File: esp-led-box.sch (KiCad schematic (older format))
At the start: 26 parts, among them J1 Conn_01x03, J2 Conn_01x02_Female, J3 Conn_01x03_Female, Q1 BSS138, U1 ESP-12F, U2 MP2307, U3 LM3940

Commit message: Fixed iteration #2
- replace 0603 SMDs with 1206 ones;
- add fuse holder
- add two ACT LEDs
- fix level shifter transistor scheme
- add degson terminal block
- use 2.56 pin header
- add GPIO0, +3.3v pins to pin header
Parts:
- added D1, D2: LED, LED_SMD:LED_1206_3216Metric, symbol Device:LED
- added D3: D, Diode_SMD:D_SOD-123, symbol Device:D
- added F1: Fuse, Fuse:Fuseholder_Blade_Mini_Keystone_3568, symbol Device:Fuse
- added R11, R12: 120, Resistor_SMD:R_1206_3216Metric, symbol Device:R
- C2, C4, C5, C6: footprint Capacitor_SMD:C_0603_1608Metric -> Capacitor_SMD:C_1206_3216Metric
- J1: footprint Connector_PinHeader_1.27mm:PinHeader_1x04_P1.27mm_Vertical -> Connector_PinHeader_2.54mm:PinHeader_1x06_P2.54mm_Vertical; symbol Connector_Generic:Conn_01x04 -> Connector_Generic:Conn_01x06
- J2: footprint Connector_PinHeader_1.27mm:PinHeader_1x02_P1.27mm_Vertical -> esp-light-box:WG235-2P
- J3: footprint Connector_PinHeader_1.27mm:PinHeader_1x03_P1.27mm_Vertical -> Connector_PinHeader_2.54mm:PinHeader_1x03_P2.54mm_Vertical
- R1, R10, R2, R3, R4, R5, R6, R7, R8, R9: footprint Resistor_SMD:R_0603_1608Metric -> Resistor_SMD:R_1206_3216Metric
- U1: symbol ESP8266:ESP-12F -> esp-led-box-rescue:ESP-12F-ESP8266
- U2: symbol mp2307:MP2307 -> esp-led-box-rescue:MP2307-mp2307
- U3: symbol lm3940:LM3940 -> esp-led-box-rescue:LM3940-lm3940
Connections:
- net labels added: GPIO0, GREEN_LED, RED_LED
- wire segments 60 -> 74
- no-connect marks 14 -> 12
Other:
- moved on the sheet: J2, Q1, R10, R3, R9

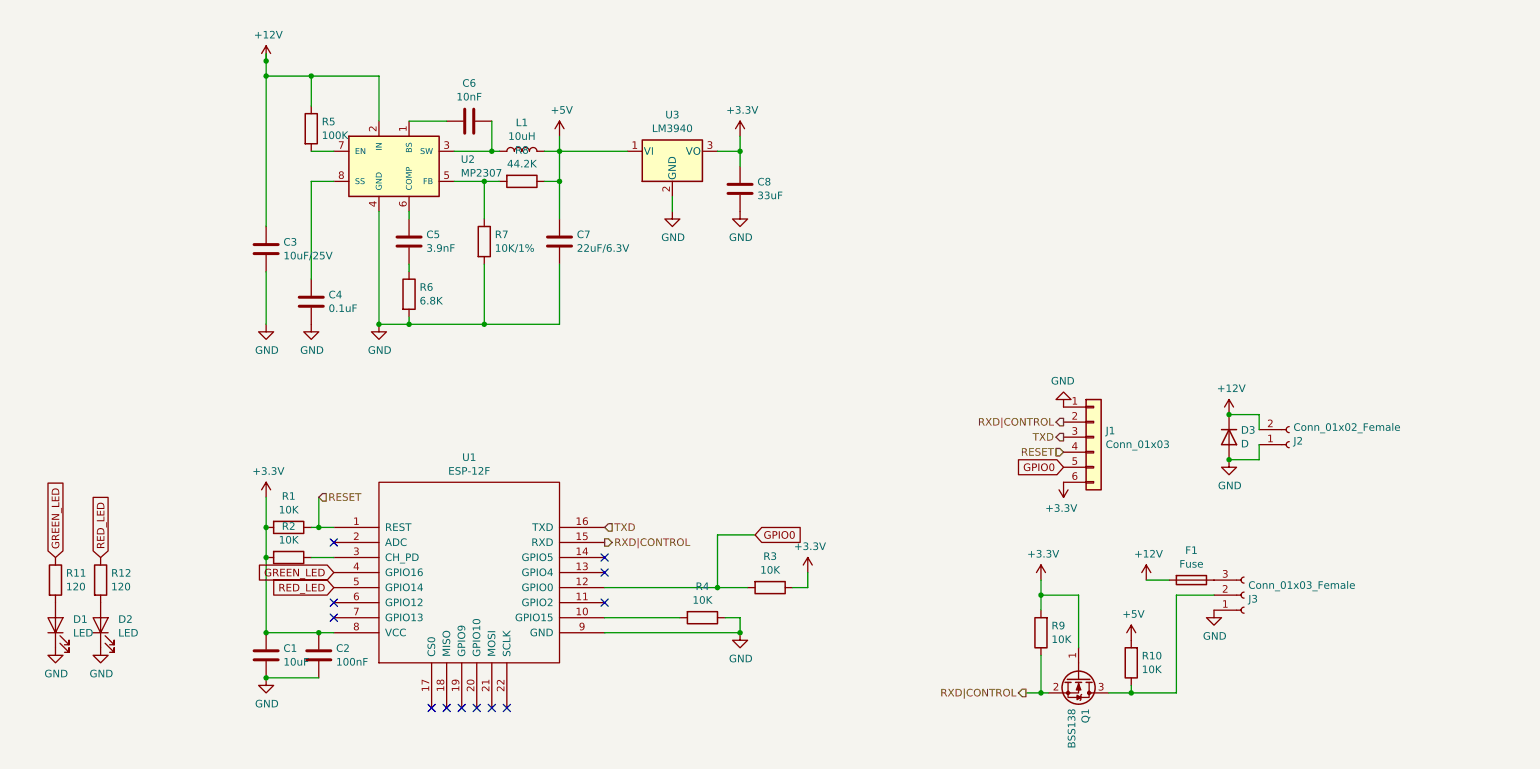
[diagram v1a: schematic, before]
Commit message: pcb: make ready for manufacturing
- dummy resistors to switch from +12v power input to +5v input to make box be usable with different LED strips
- some cosmetic changes withing .sch
- put protection diode inline not parallel
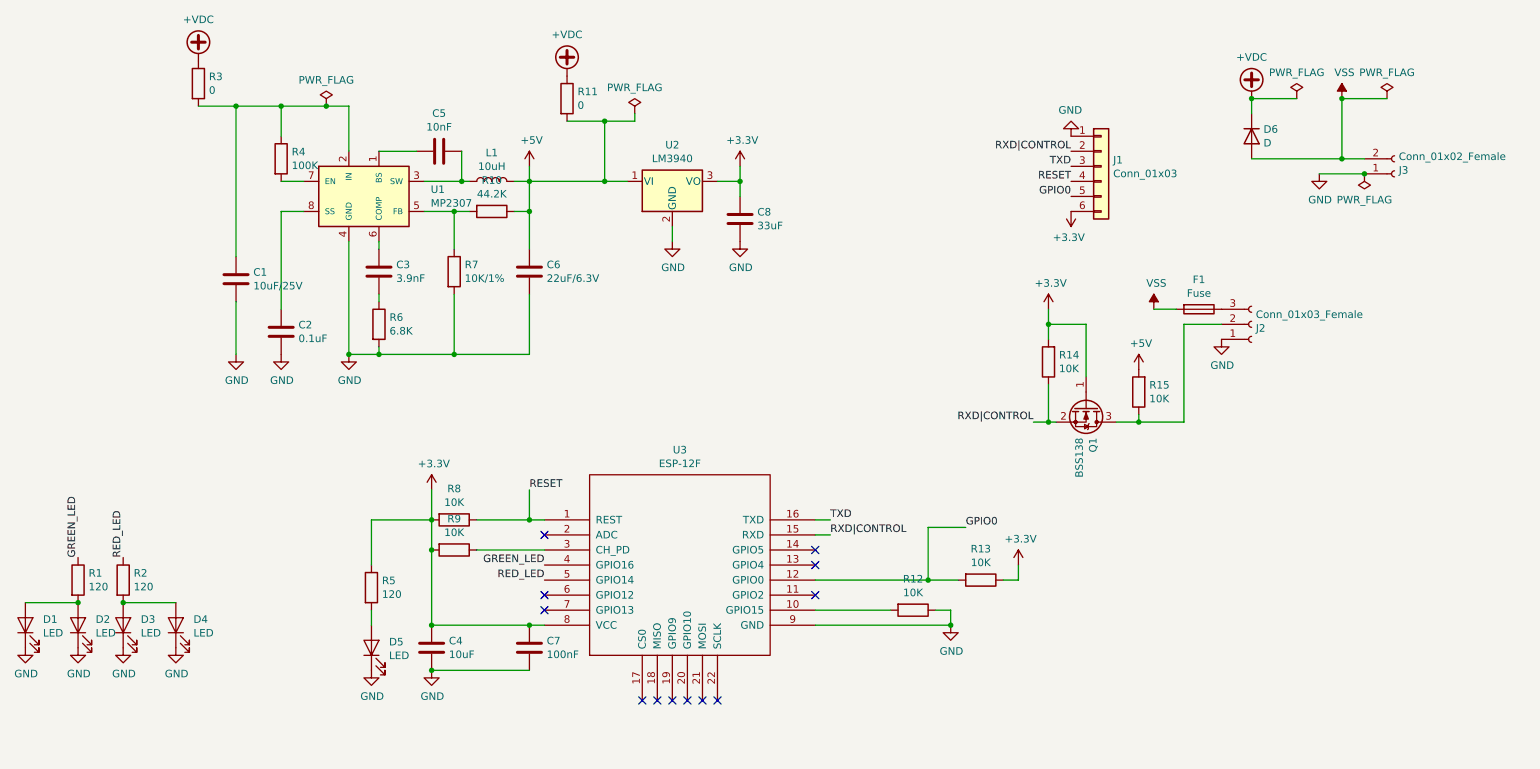
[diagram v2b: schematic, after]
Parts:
- added D1, D4, D5: LED, LED_SMD:LED_1206_3216Metric, symbol Device:LED
- added R11, R3: 0, Resistor_SMD:R_1206_3216Metric, symbol Device:R
- added R5: 120, Resistor_SMD:R_1206_3216Metric, symbol Device:R
- renumbered C3 to C1, C4 to C2, C5 to C3, C1 to C4, C6 to C5, C7 to C6, C2 to C7, D1 to D2, D2 to D3, D3 to D6, J3 to J2, J2 to J3, R11 to R1, R8 to R10, R4 to R12, R3 to R13, R9 to R14, R10 to R15, R12 to R2, R5 to R4, R1 to R8, R2 to R9, U2 to U1, U3 to U2, U1 to U3
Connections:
- net +3V3: now also R5.1
- net +5V: now also R11.2
- net GND: now also D1.1 (K), D4.1 (K), D5.1 (K); no longer D6.2 (A)
- net at D2.2 (A), R1.2: now also D1.2 (A)
- net at D3.2 (A), R2.2: now also D4.2 (A)
- net +12V: no longer names the net of C1.1, R4.1, U1.2 (IN)
- net +12V: now also R3.2; no longer D6.1 (K), F1.2, J3.2 (Pin_2)
- new net: D5.2 (A), R5.2
- new net +VDC: D6.1 (K), R11.1, R3.1
- new net VSS: D6.2 (A), F1.2, J3.2 (Pin_2)
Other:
- moved on the sheet: C1, C2, C3, C4, C5, C6, C7, C8, D2, D3, D6, F1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

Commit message: rework fuse holder: use one from aliexpress
https://aliexpress.ru/item/32838425418.html?spm=a2g0s.9042311.0.0.5f9933edQqCEM1 here is the link (it supposed to be used with micro blades fuses)
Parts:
- F1: footprint Fuse:Fuseholder_Blade_Mini_Keystone_3568 -> esp-light-box:fuseholder_blade_common_aliexpress
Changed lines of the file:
@@
 	1    0    0    -1
-$EndComp
-$Comp
-L Device:Fuse F1
-U 1 1 5E6D1E06
-P 8500 2800
-F 0 "F1" V 8303 2800 50  0000 C CNN
-F 1 "Fuse" V 8394 2800 50  0000 C CNN
-F 2 "Fuse:Fuseholder_Blade_Mini_Keystone_3568" V 8430 2800 50  0001 C CNN
-F 3 "~" H 8500 2800 50  0001 C CNN
-	1    8500 2800
-	0    1    1    0
 $EndComp
 Wire Wire Line
@@
 	4050 1950 4550 1950
 $Comp
-L power:VSS #PWR?
+L power:VSS #PWR0101
 U 1 1 5E906664
 P 9450 1400
-F 0 "#PWR?" H 9450 1250 50  0001 C CNN
+F 0 "#PWR0101" H 9450 1250 50  0001 C CNN
 F 1 "VSS" H 9467 1573 50  0000 C CNN
 F 2 "" H 9450 1400 50  0001 C CNN
@@
 $EndComp
 $Comp
-L power:PWR_FLAG #FLG?
+L power:PWR_FLAG #FLG0101
 U 1 1 5E907205
 P 9750 1400
-F 0 "#FLG?" H 9750 1475 50  0001 C CNN
+F 0 "#FLG0101" H 9750 1475 50  0001 C CNN
 F 1 "PWR_FLAG" H 9750 1573 50  0000 C CNN
 F 2 "" H 9750 1400 50  0001 C CNN
@@
 $EndComp
 $Comp
-L power:VSS #PWR?
+L power:VSS #PWR0102
 U 1 1 5E919360
 P 8200 2800
-F 0 "#PWR?" H 8200 2650 50  0001 C CNN
+F 0 "#PWR0102" H 8200 2650 50  0001 C CNN
 F 1 "VSS" H 8217 2973 50  0000 C CNN
 F 2 "" H 8200 2800 50  0001 C CNN
@@
 	1    0    0    -1
 $EndComp
+$Comp
+L Device:Fuse F1
+U 1 1 5E6D1E06
+P 8500 2800
+F 0 "F1" V 8303 2800 50  0000 C CNN
+F 1 "Fuse" V 8394 2800 50  0000 C CNN
+F 2 "esp-light-box:fuseholder_blade_common_aliexpress" V 8430 2800 50  0001 C CNN
+F 3 "~" H 8500 2800 50  0001 C CNN
+	1    8500 2800
+	0    1    1    0
+$EndComp
 $EndSCHEMATC

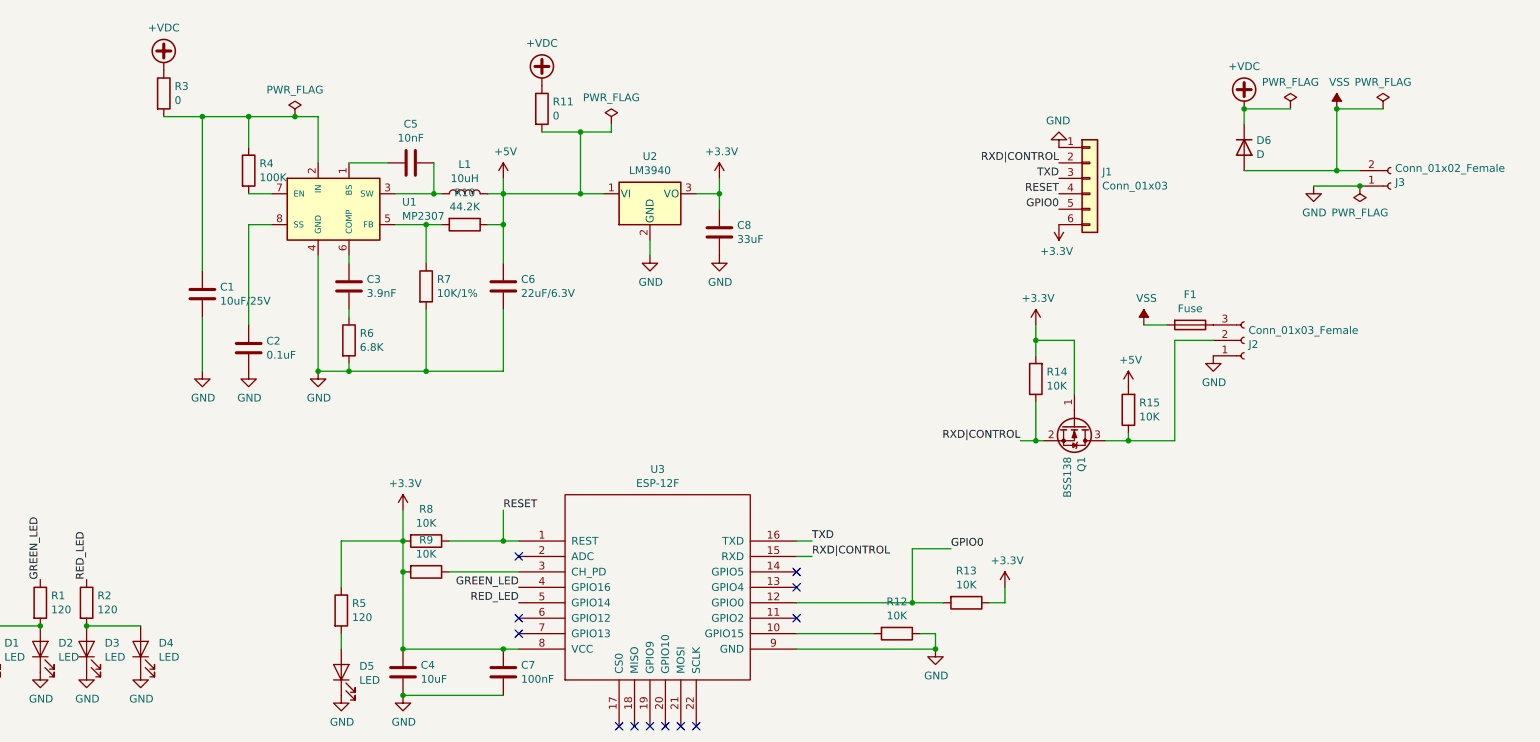
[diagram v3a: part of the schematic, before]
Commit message: pcb v0.3 update
- add possibility to use switch instead of dummy resisters
- add micro USB footprint for portable use
- add buttons for RESET and GPIO0 ESP inputs
- make it fancier with components density increased
- add case mountpoints
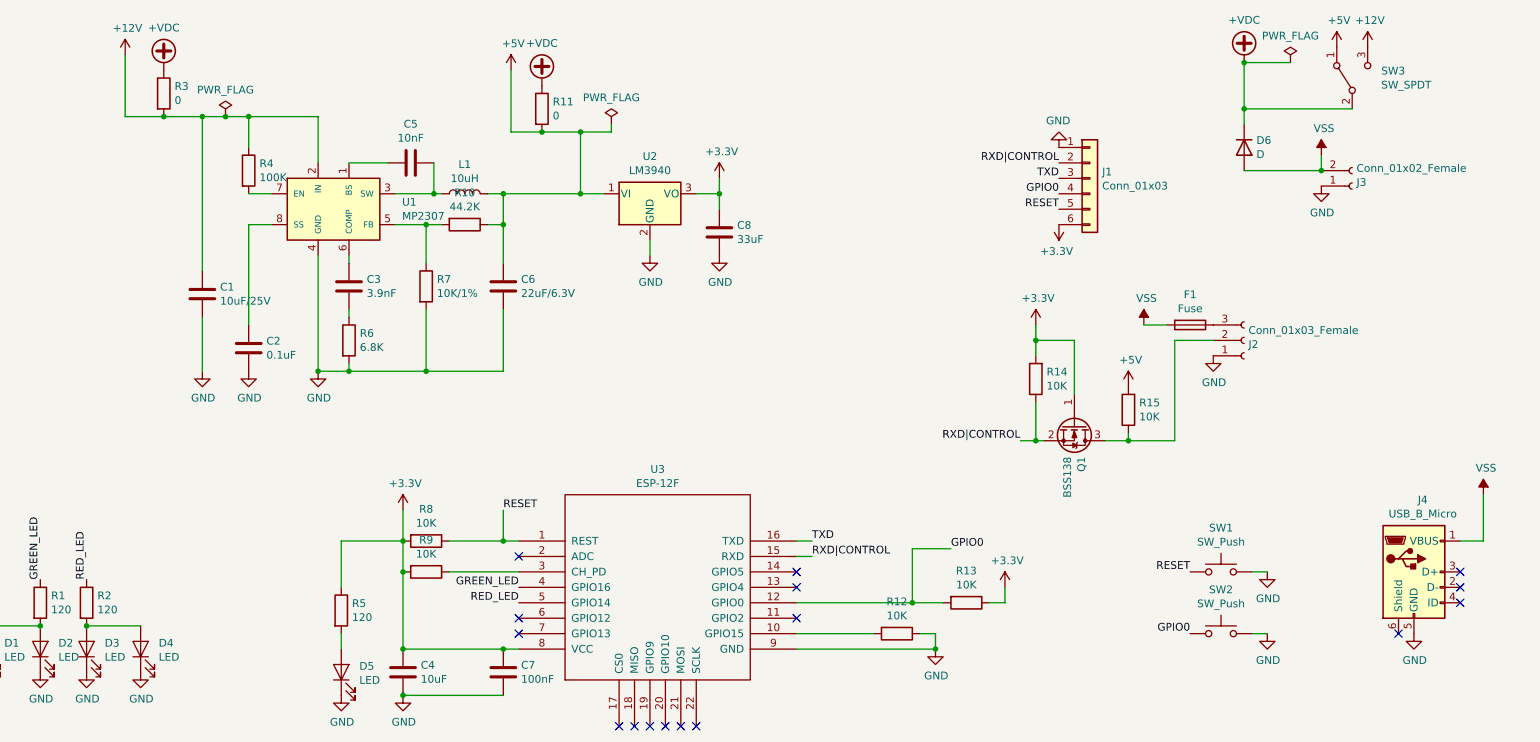
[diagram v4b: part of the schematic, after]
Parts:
- added J4: USB_B_Micro, Connector_USB:USB_Micro-B_Molex-105017-0001, symbol Connector:USB_B_Micro
- added SW1, SW2: SW_Push, Button_Switch_SMD:SW_SPST_CK_RS282G05A3, symbol Switch:SW_Push
- added SW3: SW_SPDT, Button_Switch_SMD:SW_SPDT_CK-JS102011SAQN, symbol Switch:SW_SPDT
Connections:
- net +5V: now also SW3.1 (A)
- net +VDC: now also SW3.2 (B)
- net GND: now also J4.5 (GND), SW1.2, SW2.2
- net GPIO0: now also J1.4 (Pin_4), SW2.1; no longer J1.5 (Pin_5)
- net RESET: now also J1.5 (Pin_5), SW1.1; no longer J1.4 (Pin_4)
- net VSS: now also J4.1 (VBUS)
- net +12V: now reaches C1.1, R3.2, R4.1, U1.2 (IN)
- net +12V: now also SW3.3 (C)
- no-connect marks 12 -> 16
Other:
- moved on the sheet: J3

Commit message: pre-version: still needs to fix some problems and breadboard it
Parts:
- removed C1: 10uF/25V, Capacitor_SMD:C_1210_3225Metric, symbol Device:C
- removed D5: LED, LED_SMD:LED_1206_3216Metric, symbol Device:LED
- removed D6: D, Diode_SMD:D_SOD-123, symbol Device:D
- removed SW1, SW2: SW_Push, Button_Switch_SMD:SW_SPST_CK_RS282G05A3, symbol Switch:SW_Push
- removed SW3: SW_SPDT, Button_Switch_SMD:SW_SPDT_CK-JS102011SAQN, symbol Switch:SW_SPDT
- added C1: 10u/25V, symbol Device:CP
- added C10: 1uF, symbol Device:C
- added C11: 1u, symbol Device:C
- added C9: 1m, symbol Device:CP
- added IC1: CP2105-F01-GMR, QFN50P400X400X80-25N-D, symbol CP2105-F01-GMR:CP2105-F01-GMR
- added Q10, Q11, Q13, Q5, Q6, Q8, Q9: Q_PMOS_DGS, symbol Device:Q_PMOS_DGS
- added Q12, Q7: Q_NMOS_DGS, symbol Device:Q_NMOS_DGS
- added Q14, Q15: S8050, Package_TO_SOT_THT:TO-92_Inline, symbol Transistor_BJT:S8050
- added Q2: Q_NMOS, symbol Device:Q_DUAL_NMOS_S1G1D2S2G2D1
- added Q3: Q_DUAL_PMOS_G1S2G2D2S1D1, symbol Device:Q_DUAL_PMOS_G1S2G2D2S1D1
- added Q4: Q_P, symbol Device:Q_DUAL_PMOS_G1S2G2D2S1D1
- added R16, R19: 10k, Resistor_SMD:R_1206_3216Metric, symbol Device:R
- added R17, R18, R20, R21: 10K, Resistor_SMD:R_1206_3216Metric, symbol Device:R
- added R22: 4.7K, symbol Device:R
- added R23, R24: 300, symbol Device:R
- added R25, R26: 12K, symbol Device:R
- added U4: TL431DBZ, Package_TO_SOT_SMD:SOT-23, symbol Reference_Voltage:TL431DBZ
- added U5: LM211, symbol Comparator:LM311
- R11: value 0 -> 10K
- R3: value 0 -> 1k
- R5: value 120 -> 24K
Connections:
- net +12V: now also C1.1, Q4.6 (D); no longer R3.2
- net +3V3: now also C10.1, IC1.5 (VIO), IC1.6 (VDD), IC1.7 (REGIN), R22.1; no longer R13.1, R5.1, R8.2
- net +5V: now also Q6.3 (S), Q8.3 (S), Q9.3 (S); no longer C6.1, L1.2, R10.1, R11.2
- net GND: now also J4.6 (Shield), R8.2, C1.2, C10.2, C11.1, C9.2, IC1.2 (GND), Q11.2 (G), Q2.1 (S), Q5.2 (G), Q6.2 (G), Q8.2 (G), Q9.2 (G), R17.1, R20.1, U4.3 (A), U5.1 (GND), U5.4 (V-)
- net GPIO0: now also Q14.3 (C); no longer R13.2
- net RESET: now also Q15.1 (E); no longer R8.1
- net RXD|CONTROL: now also R23.2
- net TXD: now also R24.2
- net at R5.2: now also R8.1, U5.2 (+)
- net D-: now reaches J4.2 (D-)
- net D-: now also IC1.4 (D-)
- net D+: now reaches J4.3 (D+)
- net D+: now also IC1.3 (D+)
- net +VDC: no longer names the net of R3.1
- net +VDC: now also U4.1 (K), U4.2 (REF), U5.3 (-); no longer R11.1
- net GREEN_LED renamed GRN_LED
- removed net VSS: F1.2, J3.2 (Pin_2), J4.1 (VBUS)
- new net: Q2.2 (G), Q4.1 (G), R11.2, U5.7
- new net: Q2.6 (D), Q3.1 (G), R13.2
- new net: Q12.3 (S), R20.2, R21.1
- new net: Q13.2 (G), R21.2
- new net: IC1.20 (RXD_SCI), R24.1
- new net: IC1.21 (TXD_SCI), R23.1
- new net: IC1.9 (~RST), R22.2
- new net: Q14.2 (B), R25.2
- new net: Q15.2 (B), R26.2
- new net: Q11.3 (S), Q12.1 (D), Q13.1 (D)
- new net: Q12.2 (G), R19.2
- new net: Q7.2 (G), R16.2
- new net: Q7.3 (S), R17.2, R18.1
- new net: Q10.2 (G), R18.2
- new net: U5.5 (BAL), U5.6 (STRB)
- new net BUCK_5V: C6.1, L1.2, Q6.1 (D), R10.1
- new net DC_5V: Q3.6 (D), Q9.1 (D)
- new net DTR: IC1.23 (GPIO.1_SCI_/_DTR_SCI), Q15.3 (C), R25.1
- new net LED_PWR: F1.2, Q10.3 (S), Q5.3 (S)
- new net RTS: IC1.19 (RTS_SCI), Q14.1 (E), R26.1
- new net VBUS: C11.2, IC1.8 (VBUS), J4.1 (VBUS), Q10.1 (D), Q7.1 (D), Q8.1 (D), R19.1
- new net VDC: C9.1, J3.2 (Pin_2), Q11.1 (D), Q5.1 (D), R16.1
- new net VDD: Q13.3 (S), Q3.5 (S), Q4.5 (S), R11.1, R13.1, R3.2, R5.1, U5.8 (V+)
- no-connect marks 16 -> 26
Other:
- moved on the sheet: C2, C3, C4, C5, C6, C7, C8, D1, D2, D3, D4, F1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
